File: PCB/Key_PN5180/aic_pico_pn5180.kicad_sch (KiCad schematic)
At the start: 34 parts, among them J1 Conn_01x02_Female, J2 PN5180, SW1 SKRR_4pin, SW10 SKRR_4pin, SW11 SKRR_4pin, SW12 SKRR_4pin, SW2 SKRR_4pin, SW3 SKRR_4pin, SW4 SKRR_4pin, SW5 SKRR_4pin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

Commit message: Power filtering for PN5180 on AIC Key
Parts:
- added C1: 0.1uF, Capacitor_SMD:C_0603_1608Metric, symbol Device:C
- added C2: 10uF, Capacitor_SMD:C_0603_1608Metric, symbol Device:C
- added L1: 100nH, Inductor_SMD:L_0805_2012Metric, symbol Device:L
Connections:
- net +5V: now also L1.1; no longer J2.1 (5V)
- net GND: now also C1.2, C2.2
- new net: C1.1, C2.1, J2.1 (5V), L1.2
- no-connect marks 11 -> 12
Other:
- moved on the sheet: J1

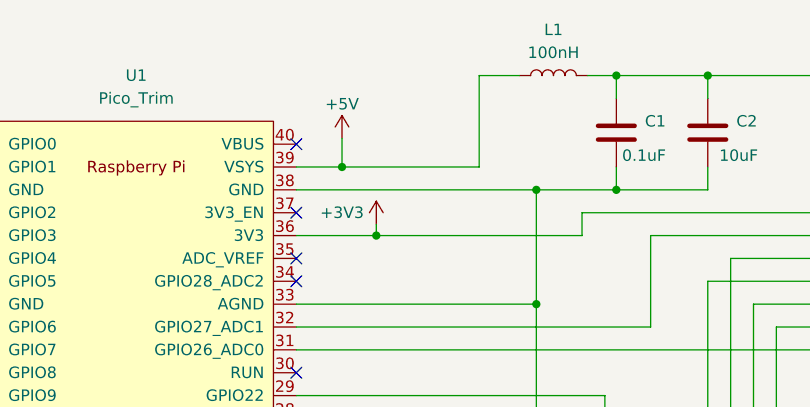
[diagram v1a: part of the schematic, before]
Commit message: L1 to 1206 and power from VBUS
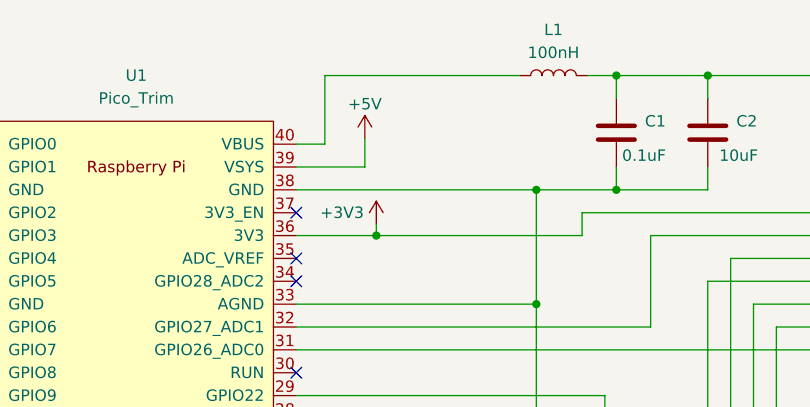
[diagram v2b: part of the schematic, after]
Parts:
- L1: footprint Inductor_SMD:L_0805_2012Metric -> Inductor_SMD:L_1206_3216Metric
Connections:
- net +5V: no longer L1.1
- net at U1.40 (VBUS): now also L1.1
- no-connect marks 12 -> 11
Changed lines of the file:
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@@
   (junction (at 165.1 171.45) (diameter 0) (color 0 0 0 0)
   )
-  (junction (at 214.63 78.74) (diameter 0) (color 0 0 0 0)
-  )
   (junction (at 63.5 99.06) (diameter 0) (color 0 0 0 0)
   )
@@
   (junction (at 80.01 99.06) (diameter 0) (color 0 0 0 0)
   )
-  (no_connect (at 209.55 76.2))
   (no_connect (at 279.4 106.68))
   (no_connect (at 279.4 109.22))
@@
     (stroke (width 0) (type default))
   )
-  (wire (pts (xy 229.87 68.58) (xy 234.315 68.58))
+  (wire (pts (xy 212.725 68.58) (xy 234.315 68.58))
     (stroke (width 0) (type default))
   )
@@
     (stroke (width 0) (type default))
   )
+  (wire (pts (xy 212.725 76.2) (xy 209.55 76.2))
+    (stroke (width 0) (type default))
+  )
   (wire (pts (xy 80.01 120.65) (xy 80.01 127))
     (stroke (width 0) (type default))
@@
     (stroke (width 0) (type default))
   )
+  (wire (pts (xy 212.725 76.2) (xy 212.725 68.58))
+    (stroke (width 0) (type default))
+  )
   (wire (pts (xy 203.2 189.23) (xy 203.2 191.77))
     (stroke (width 0) (type default))
@@
     (stroke (width 0) (type default))
   )
-  (wire (pts (xy 214.63 78.74) (xy 209.55 78.74))
+  (wire (pts (xy 217.17 78.74) (xy 209.55 78.74))
     (stroke (width 0) (type default))
   )
@@
     (stroke (width 0) (type default))
   )
-  (wire (pts (xy 214.63 78.74) (xy 229.87 78.74))
-    (stroke (width 0) (type default))
-  )
   (wire (pts (xy 262.89 116.84) (xy 262.89 96.52))
     (stroke (width 0) (type default))
@@
     (stroke (width 0) (type default))
   )
-  (wire (pts (xy 229.87 68.58) (xy 229.87 78.74))
-    (stroke (width 0) (type default))
-  )
   (wire (pts (xy 142.24 151.13) (xy 158.75 151.13))
     (stroke (width 0) (type default))
@@
     (stroke (width 0) (type default))
   )
-  (wire (pts (xy 214.63 75.565) (xy 214.63 78.74))
+  (wire (pts (xy 217.17 75.565) (xy 217.17 78.74))
     (stroke (width 0) (type default))
   )
@@
     (effects (font (size 1.27 1.27)) (justify right bottom))
   )
-  (symbol (lib_id "power:+5V") (at 214.63 75.565 0) (unit 1)
-    (in_bom yes) (on_board yes) (dnp no)
-    (property "Reference" "#PWR0114" (at 214.63 79.375 0)
-      (effects (font (size 1.27 1.27)) hide)
-    )
-    (property "Value" "+5V" (at 214.63 71.755 0)
-      (effects (font (size 1.27 1.27)))
-    )
-    (property "Footprint" "" (at 214.63 75.565 0)
-      (effects (font (size 1.27 1.27)) hide)
-    )
-    (property "Datasheet" "" (at 214.63 75.565 0)
+  (symbol (lib_id "power:+5V") (at 217.17 75.565 0) (unit 1)
+    (in_bom yes) (on_board yes) (dnp no)
+    (property "Reference" "#PWR0114" (at 217.17 79.375 0)
+      (effects (font (size 1.27 1.27)) hide)
+    )
+    (property "Value" "+5V" (at 217.17 71.755 0)
+      (effects (font (size 1.27 1.27)))
+    )
+    (property "Footprint" "" (at 217.17 75.565 0)
+      (effects (font (size 1.27 1.27)) hide)
+    )
+    (property "Datasheet" "" (at 217.17 75.565 0)
       (effects (font (size 1.27 1.27)) hide)
     )
@@
       (effects (font (size 1.27 1.27)))
     )
-    (property "Footprint" "Inductor_SMD:L_0805_2012Metric" (at 238.125 68.58 0)
-      (effects (font (size 1.27 1.27)) hide)
-    )
+    (property "Footprint" "Inductor_SMD:L_1206_3216Metric" (at 238.125 68.58 0)
+      (effects (font (size 1.27 1.27)) hide)
+    )
